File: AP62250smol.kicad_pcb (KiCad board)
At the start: 2 copper layers, 20.3 x 10.2 mm, 13 parts, among them J1 Heatsink Pads, J2 Connector Pads, U1 AP62250Z6

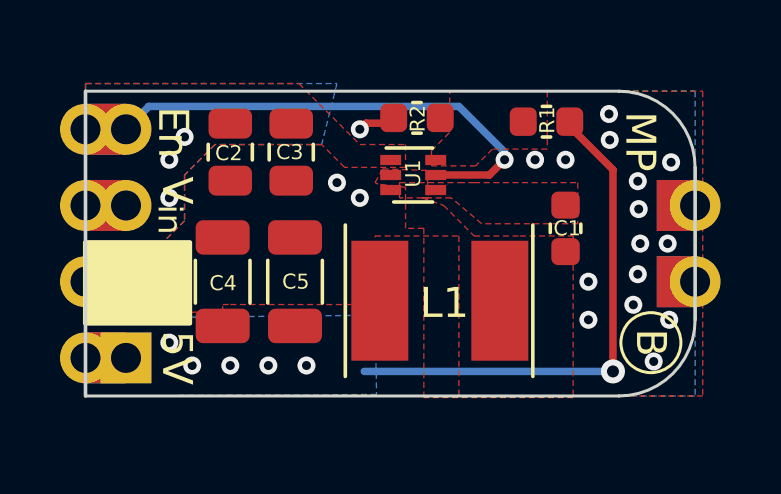
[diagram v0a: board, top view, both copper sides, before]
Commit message: I am a liar who lies. This is RevB. Major revision changes board dimensions and increases input capacitor to 1206
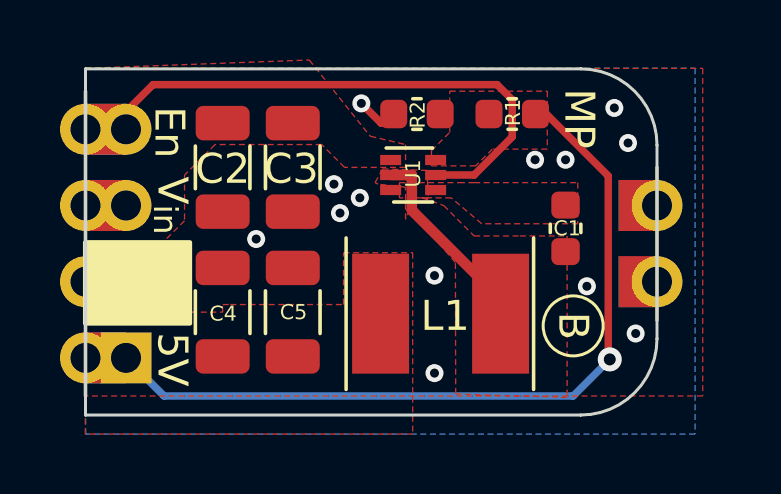
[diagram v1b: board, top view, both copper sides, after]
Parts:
- C2, C3: footprint Capacitor_SMD:C_0805_2012Metric -> Capacitor_SMD:C_1206_3216Metric
- moved MISC1 2.65 mm to (140.7, 91.6)
- moved J1 1.27 mm to (141.0, 90.2)
- moved R1 1.17 mm to (138.7, 84.6)
- moved C5 1.02 mm to (131.4, 91.2)
- moved C4 1.02 mm to (129.0, 91.2)
- moved C2 0.57 mm to (129.0, 86.4)
- moved C3 0.51 mm to (131.4, 86.4)
- moved L1 0.43 mm to (136.3, 91.2)
- moved R2 0.13 mm to (135.5, 84.6)
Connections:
- net +12V renamed V_{IN}
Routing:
- net +5V: track 17.1 -> 26.6 mm, vias 6 -> 1
- net Net-(C1-Pad1): track 0.00 -> 6.06 mm
- net En: track 16.3 -> 17.8 mm, vias 1 -> 0
- net GND: track 1.04 -> 1.17 mm, vias 20 -> 15
- net V_{IN}: vias 3 -> 0
- removed copper zone on B.Cu, net +5V
- removed copper zone on B.Cu, net V_{IN}
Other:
- board size 20.3 x 10.2 mm -> 19 x 11.5 mm
- board text added: "5V 2A Out"
- board text added: "7-18V In"
- board text removed: "Max 18V In"
- board text removed: "Out 5V 2A"

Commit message: Removed second input capacitor.
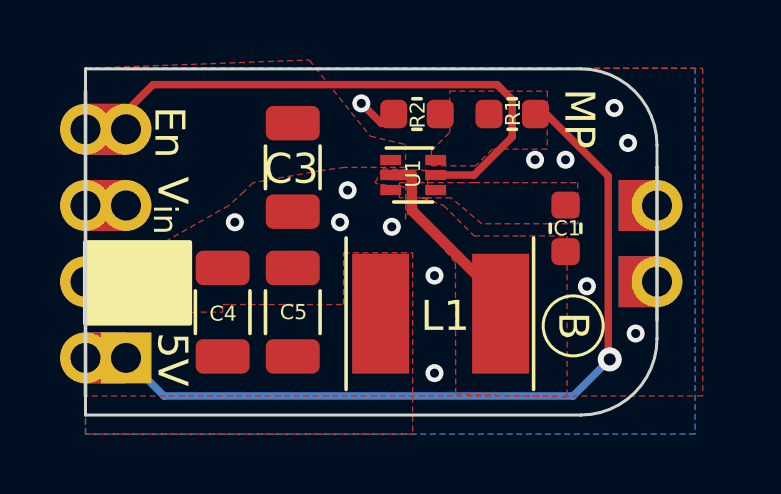
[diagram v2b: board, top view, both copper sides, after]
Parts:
- removed C2: 10uF_Opt, Capacitor_SMD:C_1206_3216Metric
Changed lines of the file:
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@@
   (net 6 "En")
   (net 7 "+5V")
-  (footprint "Capacitor_SMD:C_1206_3216Metric" (layer "F.Cu")
-    (at 129.032 86.36 -90)
-    (descr "Capacitor SMD 1206 (3216 Metric), square (rectangular) end terminal, IPC_7351 nominal, (Body size source: IPC-SM-782 page 76, https://www.pcb-3d.com/wordpress/wp-content/uploads/ipc-sm-782a_amendment_1_and_2.pdf), generated with kicad-footprint-generator")
-    (tags "capacitor")
-    (property "Sheetfile" "AP62250smol.kicad_sch")
-    (property "Sheetname" "")
-    (property "exclude_from_bom" "")
-    (attr smd exclude_from_bom)
-    (fp_text reference "C2" (at 0.0508 0) (layer "F.SilkS")
-      (effects (font (size 1 1) (thickness 0.15)))
-    )
-    (fp_text value "10uF_Opt" (at 0 1.85 -90) (layer "F.Fab")
-      (effects (font (size 1 1) (thickness 0.15)))
-    )
-    (fp_text user "${REFERENCE}" (at 0 0 -90) (layer "F.Fab")
-      (effects (font (size 0.8 0.8) (thickness 0.12)))
-    )
-    (fp_line (start -0.711252 0.91) (end 0.711252 0.91) (layer "F.SilkS") (width 0.12))
-    (fp_line (start -0.711252 -0.91) (end 0.711252 -0.91) (layer "F.SilkS") (width 0.12))
-    (fp_line (start 2.3 -1.15) (end 2.3 1.15) (layer "F.CrtYd") (width 0.05))
-    (fp_line (start -2.3 1.15) (end -2.3 -1.15) (layer "F.CrtYd") (width 0.05))
-    (fp_line (start -2.3 -1.15) (end 2.3 -1.15) (layer "F.CrtYd") (width 0.05))
-    (fp_line (start 2.3 1.15) (end -2.3 1.15) (layer "F.CrtYd") (width 0.05))
-    (fp_line (start -1.6 -0.8) (end 1.6 -0.8) (layer "F.Fab") (width 0.1))
-    (fp_line (start -1.6 0.8) (end -1.6 -0.8) (layer "F.Fab") (width 0.1))
-    (fp_line (start 1.6 -0.8) (end 1.6 0.8) (layer "F.Fab") (width 0.1))
-    (fp_line (start 1.6 0.8) (end -1.6 0.8) (layer "F.Fab") (width 0.1))
-    (pad "1" smd roundrect locked (at -1.475 0 270) (size 1.15 1.8) (layers "F.Cu" "F.Paste" "F.Mask") (roundrect_rratio 0.217391)
-      (net 1 "V_{IN}") (pintype "passive"))
-    (pad "2" smd roundrect locked (at 1.475 0 270) (size 1.15 1.8) (layers "F.Cu" "F.Paste" "F.Mask") (roundrect_rratio 0.217391)
-      (net 2 "GND") (pintype "passive"))
-    (model "${KICAD6_3DMODEL_DIR}/Capacitor_SMD.3dshapes/C_1206_3216Metric.wrl"
-      (offset (xyz 0 0 0))
-      (scale (xyz 1 1 1))
-      (rotate (xyz 0 0 0))
-    )
-  )
   (footprint "MikeFootprintLib:RevisionSymbol_Small" (layer "F.Cu")
     (at 140.716 91.6432 -90)
@@
     (fp_line (start -1.6 -0.8) (end 1.6 -0.8) (layer "F.Fab") (width 0.1))
     (fp_line (start 1.6 -0.8) (end 1.6 0.8) (layer "F.Fab") (width 0.1))
-    (pad "1" smd roundrect locked (at -1.475 0 270) (size 1.15 1.8) (layers "F.Cu" "F.Paste" "F.Mask") (roundrect_rratio 0.217391)
+    (pad "1" smd roundrect locked (at -1.475 0 270) (size 1.15 1.8) (layers "F.Cu" "F.Paste" "F.Mask") (roundrect_rratio 0.2173913043)
       (net 1 "V_{IN}") (pintype "passive"))
-    (pad "2" smd roundrect locked (at 1.475 0 270) (size 1.15 1.8) (layers "F.Cu" "F.Paste" "F.Mask") (roundrect_rratio 0.217391)
+    (pad "2" smd roundrect locked (at 1.475 0 270) (size 1.15 1.8) (layers "F.Cu" "F.Paste" "F.Mask") (roundrect_rratio 0.2173913043)
       (net 2 "GND") (pintype "passive"))
     (model "${KICAD6_3DMODEL_DIR}/Capacitor_SMD.3dshapes/C_1206_3216Metric.wrl"
@@
   (via (at 142.7988 91.8972) (size 0.6) (drill 0.3) (layers "F.Cu" "B.Cu") (free) (net 2))
   (via (at 136.0932 93.218) (size 0.6) (drill 0.3) (layers "F.Cu" "B.Cu") (free) (net 2))
-  (via (at 130.1496 88.7476) (size 0.6) (drill 0.3) (layers "F.Cu" "B.Cu") (free) (net 2))
-  (via (at 132.9436 87.884) (size 0.6) (drill 0.3) (layers "F.Cu" "B.Cu") (free) (net 2))
+  (via (at 129.4384 88.1888) (size 0.6) (drill 0.3) (layers "F.Cu" "B.Cu") (free) (net 2))
+  (via (at 132.9436 88.1888) (size 0.6) (drill 0.3) (layers "F.Cu" "B.Cu") (free) (net 2))
   (via (at 142.5448 85.5472) (size 0.6) (drill 0.3) (layers "F.Cu" "B.Cu") (free) (net 2))
-  (via (at 132.7404 86.9188) (size 0.6) (drill 0.3) (layers "F.Cu" "B.Cu") (free) (net 2))
-  (via (at 133.604 87.376) (size 0.6) (drill 0.3) (layers "F.Cu" "B.Cu") (free) (net 2))
+  (via (at 133.1976 87.122) (size 0.6) (drill 0.3) (layers "F.Cu" "B.Cu") (free) (net 2))
   (via (at 127.3048 90.678) (size 0.6) (drill 0.3) (layers "F.Cu" "B.Cu") (free) (net 2))
   (via (at 127.254 89.662) (size 0.6) (drill 0.3) (layers "F.Cu" "B.Cu") (free) (net 2))
   (via (at 136.0932 89.9668) (size 0.6) (drill 0.3) (layers "F.Cu" "B.Cu") (free) (net 2))
+  (via (at 134.6708 88.3412) (size 0.6) (drill 0.3) (layers "F.Cu" "B.Cu") (free) (net 2))
   (segment (start 135.3376 86.614) (end 135.3376 87.7888) (width 0.3556) (layer "F.Cu") (net 4))
   (segment (start 134.632 86.614) (end 135.3376 86.614) (width 0.3556) (layer "F.Cu") (net 4))
@@
         (xy 135.128 86.36)
         (xy 133.096 86.36)
-        (xy 132.334 85.598)
-        (xy 128.778 85.598)
-        (xy 127.762 86.614)
-        (xy 127.762 88.138)
+        (xy 132.334 86.4616)
+        (xy 130.048 86.868)
+        (xy 129.7432 87.1728)
+        (xy 129.2352 87.63)
         (xy 127 88.9)
         (xy 124.46 88.9)

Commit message: Actually, RevC
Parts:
- MISC1: value B -> C
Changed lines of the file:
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@@
       (effects (font (size 1 1) (thickness 0.15)))
     )
-    (fp_text value "B" (at 0 0 -90 unlocked) (layer "F.SilkS")
+    (fp_text value "C" (at 0 0 -90 unlocked) (layer "F.SilkS")
       (effects (font (size 1 1) (thickness 0.2)))
     )
